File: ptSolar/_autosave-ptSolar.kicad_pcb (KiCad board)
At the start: 4 copper layers, 30 x 73.5 mm, 67 parts, among them J1 6 Pin Male Header, J2 8 Pin Male Header, Q1 BSS138, Q2 BSS138, Q3 BSS138, Q4 MMBT3904, U1 LP3985IM5-3.3/NOPB, U2 ATMega 328p-AU, U3 SA818S-V, U4 ATGM336H-5N31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

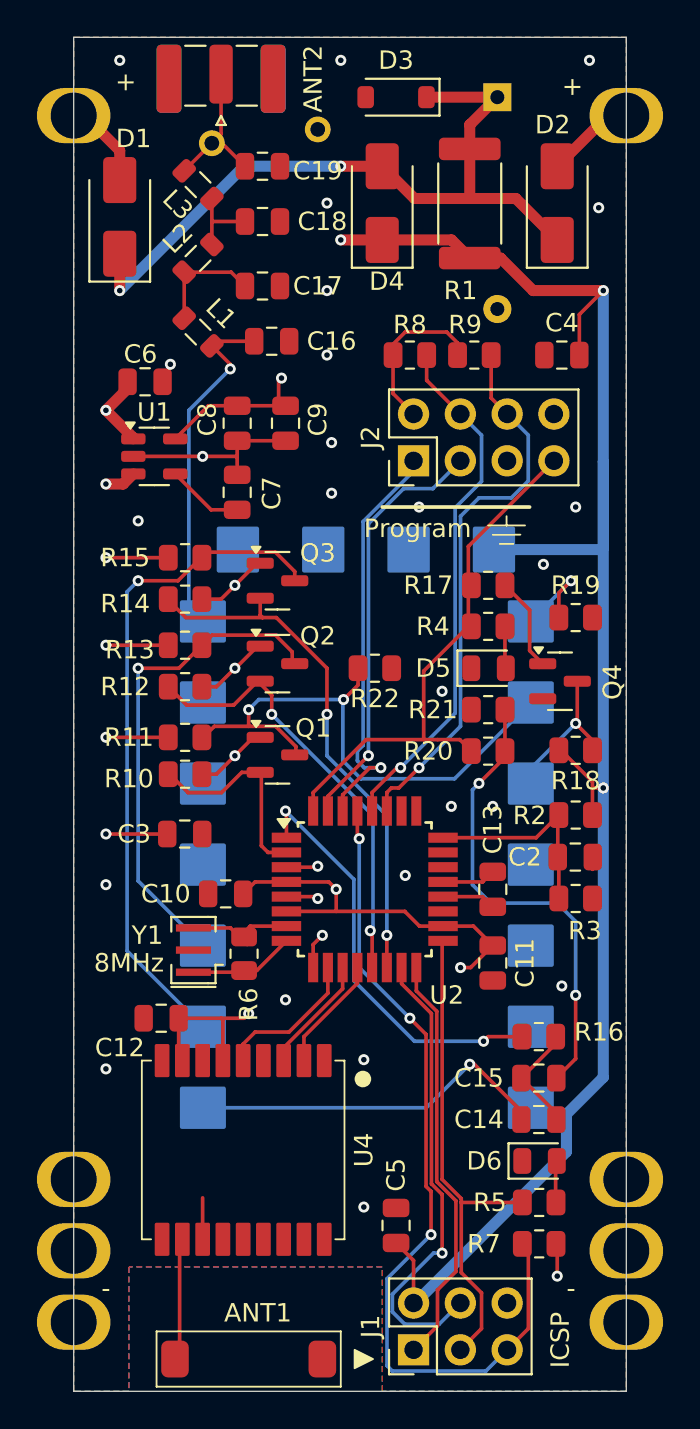
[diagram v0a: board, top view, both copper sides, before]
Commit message: Rewired GPS Enable to switch power off to GPS module
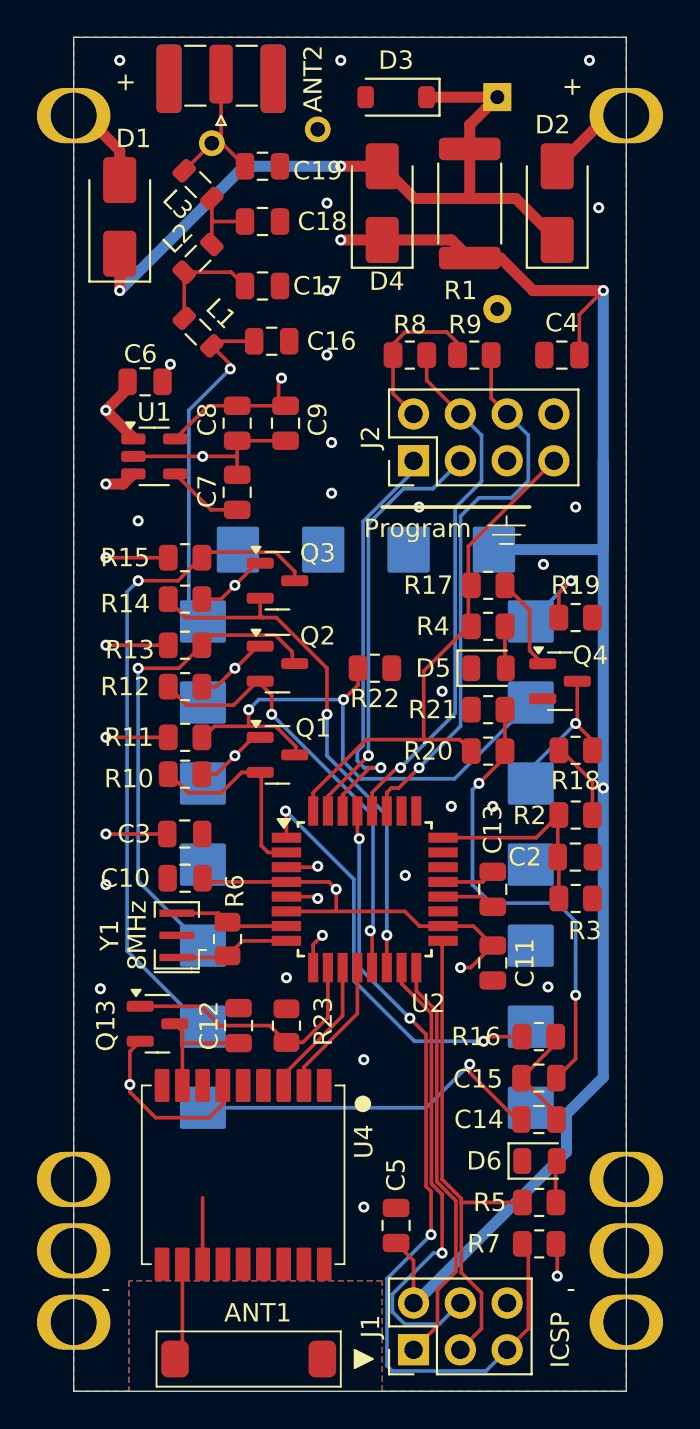
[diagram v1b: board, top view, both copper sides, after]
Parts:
- added Q13: DMP2004K-7, Package_TO_SOT_SMD:SOT-23, F.Cu at (141.8, 121.3)
- added R23: 10k, Resistor_SMD:R_0805_2012Metric, F.Cu at (148.8, 121.4)
- moved C12 4.22 mm to (146.2, 121.4), turned to 90 degrees
- moved C10 2.36 mm to (143.3, 113.4)
- moved U4 1.35 mm to (146.4, 129.7)
- moved R6 1.20 mm to (145.6, 116.7)
- moved Y1 1.20 mm to (142.8, 116.5)
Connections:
- C12 pad 1: +3.3V -> Net-(Q13-D)
- U4 pad 5: /GPS-EN -> unconnected-(U4-ON/OFF-Pad5)
- U4 pad 8: +3.3V -> Net-(Q13-D)
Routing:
- net Net-(Q13-D): track 0.00 -> 6.59 mm
- net /GPS-EN: track 8.03 -> 14.3 mm
- net +3.3V: track 60.9 -> 64.2 mm
- net /GPS-RX: track 6.25 -> 7.60 mm
- net /GPS-TX: track 6.38 -> 7.73 mm
- net GND: track 18.8 -> 20.2 mm
- net Net-(ANT1-RF): track 6.77 -> 6.02 mm
